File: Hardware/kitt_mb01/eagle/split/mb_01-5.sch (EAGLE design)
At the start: 13 parts, among them U1 TPS61032RSARPSDO-G16

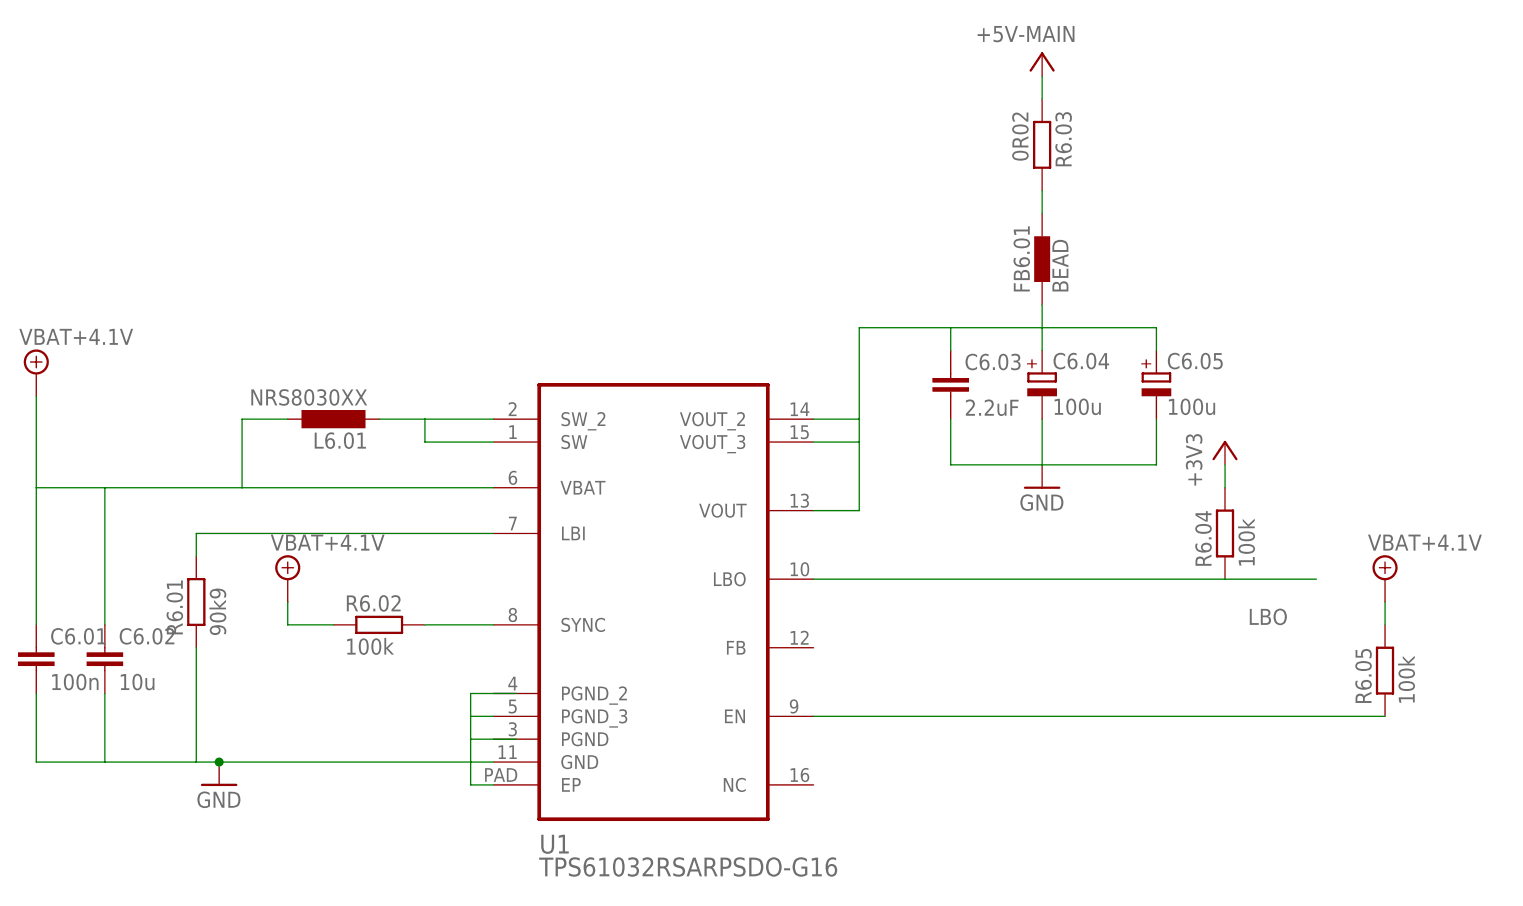
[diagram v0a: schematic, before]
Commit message: board parts 4/5 routed
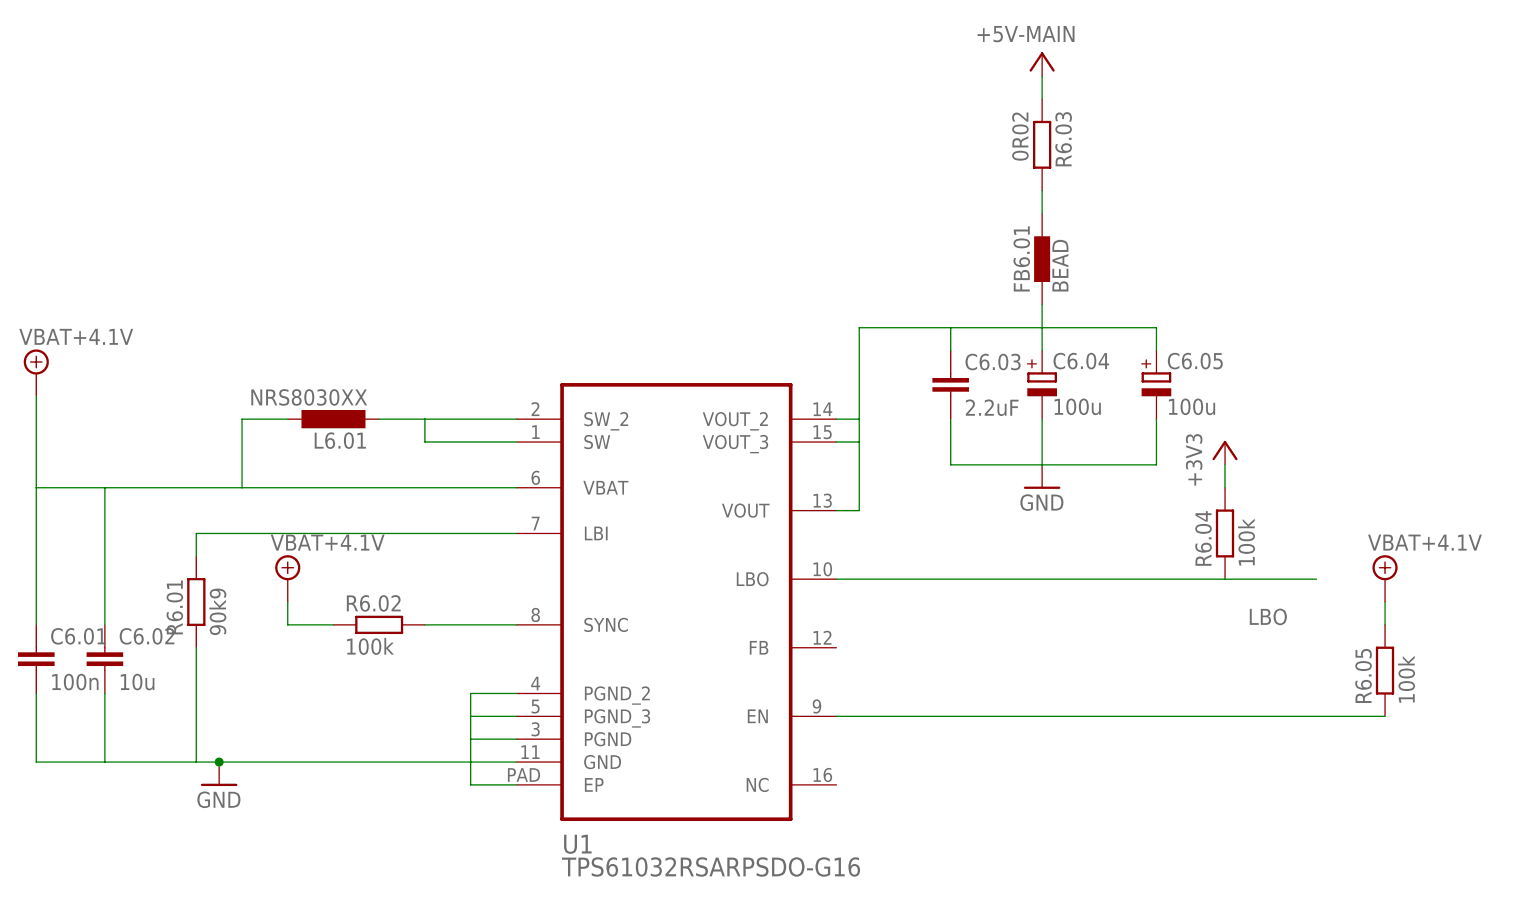
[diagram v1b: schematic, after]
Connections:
- net GND: now also C6.02.2, U1.PGND, U1.PGND_2
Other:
- moved on the sheet: U1
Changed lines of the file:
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@@
 </plain>
 <instances>
-<instance part="U1" gate="A" x="137.16" y="53.34"/>
+<instance part="U1" gate="A" x="139.7" y="53.34"/>
 <instance part="C6.03" gate="G$1" x="170.18" y="73.66"/>
 <instance part="R6.03" gate="G$1" x="180.34" y="99.06" rot="R270"/>
@@
 <segment>
 <pinref part="U1" gate="A" pin="SW_2"/>
-<wire x1="119.38" y1="68.58" x2="111.76" y2="68.58" width="0.1524" layer="91"/>
+<wire x1="121.92" y1="68.58" x2="111.76" y2="68.58" width="0.1524" layer="91"/>
 <wire x1="106.68" y1="68.58" x2="111.76" y2="68.58" width="0.1524" layer="91"/>
 <wire x1="111.76" y1="68.58" x2="111.76" y2="66.04" width="0.1524" layer="91"/>
 <pinref part="U1" gate="A" pin="SW"/>
-<wire x1="111.76" y1="66.04" x2="119.38" y2="66.04" width="0.1524" layer="91"/>
+<wire x1="111.76" y1="66.04" x2="121.92" y2="66.04" width="0.1524" layer="91"/>
 <pinref part="L6.01" gate="G$1" pin="2"/>
 </segment>
@@
 <segment>
 <pinref part="U1" gate="A" pin="LBI"/>
-<wire x1="119.38" y1="55.88" x2="86.36" y2="55.88" width="0.1524" layer="91"/>
+<wire x1="121.92" y1="55.88" x2="86.36" y2="55.88" width="0.1524" layer="91"/>
 <wire x1="86.36" y1="55.88" x2="86.36" y2="53.34" width="0.1524" layer="91"/>
 <pinref part="R6.01" gate="G$1" pin="2"/>
@@
 <segment>
 <pinref part="U1" gate="A" pin="SYNC"/>
-<wire x1="119.38" y1="45.72" x2="111.76" y2="45.72" width="0.1524" layer="91"/>
+<wire x1="121.92" y1="45.72" x2="111.76" y2="45.72" width="0.1524" layer="91"/>
 <pinref part="R6.02" gate="G$1" pin="2"/>
 </segment>
@@
 <segment>
 <pinref part="U1" gate="A" pin="VOUT_2"/>
-<wire x1="154.94" y1="68.58" x2="160.02" y2="68.58" width="0.1524" layer="91"/>
+<wire x1="157.48" y1="68.58" x2="160.02" y2="68.58" width="0.1524" layer="91"/>
 <wire x1="160.02" y1="68.58" x2="160.02" y2="66.04" width="0.1524" layer="91"/>
 <pinref part="U1" gate="A" pin="VOUT_3"/>
-<wire x1="154.94" y1="66.04" x2="160.02" y2="66.04" width="0.1524" layer="91"/>
+<wire x1="157.48" y1="66.04" x2="160.02" y2="66.04" width="0.1524" layer="91"/>
 <pinref part="U1" gate="A" pin="VOUT"/>
-<wire x1="154.94" y1="58.42" x2="160.02" y2="58.42" width="0.1524" layer="91"/>
+<wire x1="157.48" y1="58.42" x2="160.02" y2="58.42" width="0.1524" layer="91"/>
 <wire x1="160.02" y1="58.42" x2="160.02" y2="66.04" width="0.1524" layer="91"/>
 <wire x1="170.18" y1="78.74" x2="180.34" y2="78.74" width="0.1524" layer="91"/>
@@
 <pinref part="U1" gate="A" pin="EN"/>
 <pinref part="R6.05" gate="G$1" pin="1"/>
-<wire x1="154.94" y1="35.56" x2="218.44" y2="35.56" width="0.1524" layer="91"/>
+<wire x1="157.48" y1="35.56" x2="218.44" y2="35.56" width="0.1524" layer="91"/>
 </segment>
 </net>
@@
 <pinref part="U1" gate="A" pin="LBO"/>
 <pinref part="R6.04" gate="G$1" pin="1"/>
-<wire x1="154.94" y1="50.8" x2="200.66" y2="50.8" width="0.1524" layer="91"/>
+<wire x1="157.48" y1="50.8" x2="200.66" y2="50.8" width="0.1524" layer="91"/>
 <wire x1="200.66" y1="50.8" x2="210.82" y2="50.8" width="0.1524" layer="91"/>
 <label x="203.2" y="45.72" size="1.778" layer="95"/>
@@
 <wire x1="116.84" y1="38.1" x2="116.84" y2="35.56" width="0.1524" layer="91"/>
 <pinref part="U1" gate="A" pin="PGND_3"/>
-<wire x1="119.38" y1="35.56" x2="116.84" y2="35.56" width="0.1524" layer="91"/>
+<wire x1="121.92" y1="35.56" x2="116.84" y2="35.56" width="0.1524" layer="91"/>
 <wire x1="116.84" y1="35.56" x2="116.84" y2="33.02" width="0.1524" layer="91"/>
-<wire x1="116.84" y1="33.02" x2="121.92" y2="33.02" width="0.1524" layer="91"/>
 <pinref part="U1" gate="A" pin="GND"/>
-<wire x1="119.38" y1="30.48" x2="116.84" y2="30.48" width="0.1524" layer="91"/>
+<wire x1="121.92" y1="30.48" x2="116.84" y2="30.48" width="0.1524" layer="91"/>
 <wire x1="116.84" y1="30.48" x2="116.84" y2="33.02" width="0.1524" layer="91"/>
 <pinref part="U1" gate="A" pin="EP"/>
-<wire x1="119.38" y1="27.94" x2="116.84" y2="27.94" width="0.1524" layer="91"/>
+<wire x1="121.92" y1="27.94" x2="116.84" y2="27.94" width="0.1524" layer="91"/>
 <wire x1="116.84" y1="27.94" x2="116.84" y2="30.48" width="0.1524" layer="91"/>
 <wire x1="76.2" y1="38.1" x2="76.2" y2="30.48" width="0.1524" layer="91"/>
@@
 <pinref part="GND25" gate="1" pin="GND"/>
 <junction x="88.9" y="30.48"/>
+<pinref part="C6.02" gate="G$1" pin="2"/>
+<pinref part="U1" gate="A" pin="PGND"/>
+<wire x1="116.84" y1="33.02" x2="121.92" y2="33.02" width="0.1524" layer="91"/>
+<pinref part="U1" gate="A" pin="PGND_2"/>
 </segment>
 </net>
@@
 <segment>
 <pinref part="U1" gate="A" pin="VBAT"/>
-<wire x1="119.38" y1="60.96" x2="91.44" y2="60.96" width="0.1524" layer="91"/>
+<wire x1="121.92" y1="60.96" x2="91.44" y2="60.96" width="0.1524" layer="91"/>
 <wire x1="96.52" y1="68.58" x2="91.44" y2="68.58" width="0.1524" layer="91"/>
 <wire x1="91.44" y1="68.58" x2="91.44" y2="60.96" width="0.1524" layer="91"/>
